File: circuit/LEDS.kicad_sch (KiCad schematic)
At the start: 22 parts, among them U801 74HC595, U802 74HC595

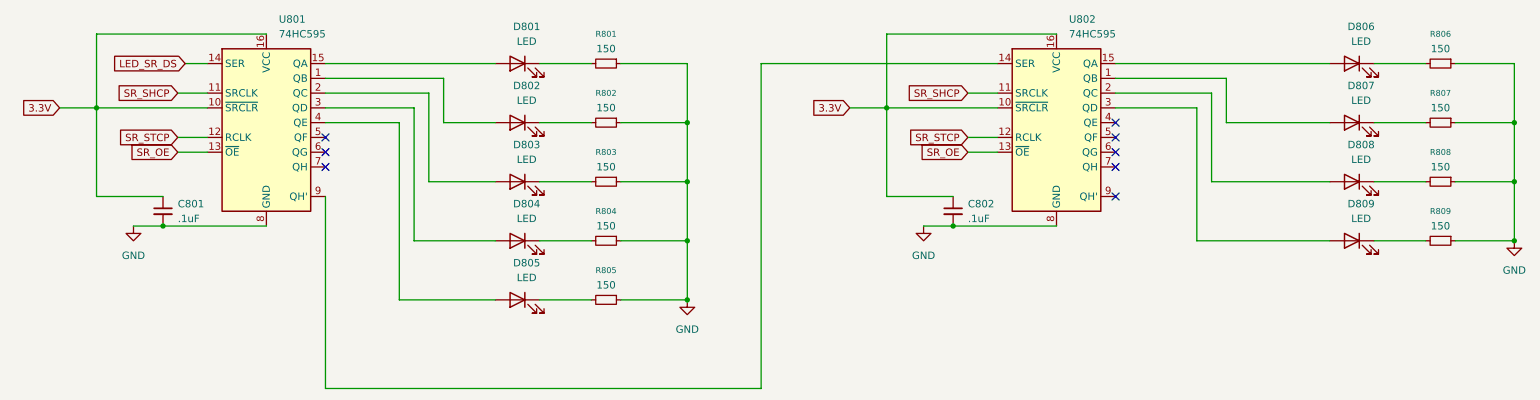
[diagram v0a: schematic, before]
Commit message: Very tentative PCB layout, Code compiles but needs major functionality testing.
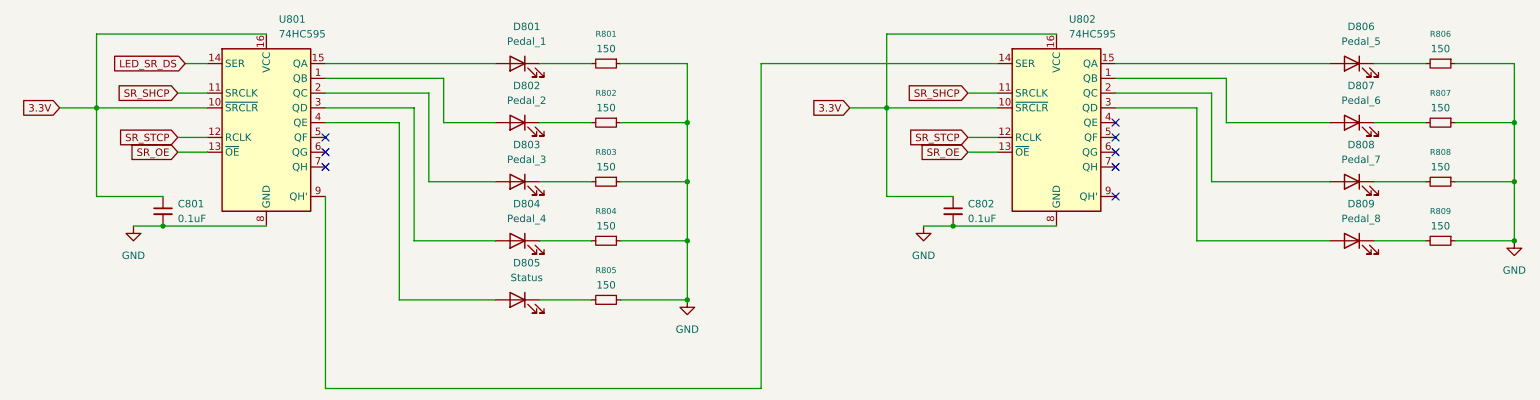
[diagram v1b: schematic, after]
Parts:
- C801, C802: value .1uF -> 0.1uF
- D801: value LED -> Pedal_1
- D802: value LED -> Pedal_2
- D803: value LED -> Pedal_3
- D804: value LED -> Pedal_4
- D805: value LED -> Status
- D806: value LED -> Pedal_5
- D807: value LED -> Pedal_6
- D808: value LED -> Pedal_7
- D809: value LED -> Pedal_8
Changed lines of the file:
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@@
 			)
 		)
-		(property "Value" "LED"
+		(property "Value" "Pedal_2"
 			(at 100.6475 72.39 0)
 			(effects
@@
 			)
 		)
-		(property "Value" ".1uF"
+		(property "Value" "0.1uF"
 			(at 40.64 92.7162 0)
 			(effects
@@
 			)
 		)
-		(property "Value" "LED"
+		(property "Value" "Pedal_7"
 			(at 244.1575 82.55 0)
 			(effects
@@
 			)
 		)
-		(property "Value" ".1uF"
+		(property "Value" "0.1uF"
 			(at 176.53 92.7162 0)
 			(effects
@@
 			)
 		)
-		(property "Value" "LED"
+		(property "Value" "Pedal_4"
 			(at 100.6475 92.71 0)
 			(effects
@@
 			)
 		)
-		(property "Value" "LED"
+		(property "Value" "Pedal_1"
 			(at 100.6475 62.23 0)
 			(effects
@@
 			)
 		)
-		(property "Value" "LED"
+		(property "Value" "Pedal_8"
 			(at 244.1575 92.71 0)
 			(effects
@@
 			)
 		)
-		(property "Value" "LED"
+		(property "Value" "Pedal_3"
 			(at 100.6475 82.55 0)
 			(effects
@@
 			)
 		)
-		(property "Value" "LED"
+		(property "Value" "Pedal_6"
 			(at 244.1575 72.39 0)
 			(effects
@@
 			)
 		)
-		(property "Value" "LED"
+		(property "Value" "Status"
 			(at 100.6475 102.87 0)
 			(effects
@@
 			)
 		)
-		(property "Value" "LED"
+		(property "Value" "Pedal_5"
 			(at 244.1575 62.23 0)
 			(effects

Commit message: Added ferrite beads and tweaked PCB
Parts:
- C801, C802: footprint Capacitor_THT:C_Axial_L3.8mm_D2.6mm_P7.50mm_Horizontal -> Capacitor_THT:C_Disc_D3.0mm_W2.0mm_P2.50mm
- D801, D802, D803, D804, D805, D806, D807, D808, D809: footprint Connector_Wire:SolderWire-0.1sqmm_1x02_P3.6mm_D0.4mm_OD1mm -> Connector_PinHeader_2.54mm:PinHeader_1x02_P2.54mm_Vertical
- R801, R802, R803, R804, R805, R806, R807, R808, R809: footprint Resistor_THT:R_Axial_DIN0204_L3.6mm_D1.6mm_P5.08mm_Horizontal -> Resistor_THT:R_Axial_DIN0207_L6.3mm_D2.5mm_P7.62mm_Horizontal
- U801, U802: footprint Package_DIP:CERDIP-16_W7.62mm_SideBrazed -> Package_DIP:DIP-16_W7.62mm
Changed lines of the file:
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@@
 			)
 		)
-		(property "Footprint" "Resistor_THT:R_Axial_DIN0204_L3.6mm_D1.6mm_P5.08mm_Horizontal"
+		(property "Footprint" "Resistor_THT:R_Axial_DIN0207_L6.3mm_D2.5mm_P7.62mm_Horizontal"
 			(at 114.3 106.68 0)
 			(effects
@@
 			)
 		)
-		(property "Footprint" "Resistor_THT:R_Axial_DIN0204_L3.6mm_D1.6mm_P5.08mm_Horizontal"
+		(property "Footprint" "Resistor_THT:R_Axial_DIN0207_L6.3mm_D2.5mm_P7.62mm_Horizontal"
 			(at 114.3 96.52 0)
 			(effects
@@
 			)
 		)
-		(property "Footprint" "Connector_Wire:SolderWire-0.1sqmm_1x02_P3.6mm_D0.4mm_OD1mm"
+		(property "Footprint" "Connector_PinHeader_2.54mm:PinHeader_1x02_P2.54mm_Vertical"
 			(at 99.06 76.2 0)
 			(effects
@@
 			)
 		)
-		(property "Description" "Light emitting diode"
+		(property "Description" ""
 			(at 99.06 76.2 0)
 			(effects
@@
 			)
 		)
-		(property "Footprint" "Resistor_THT:R_Axial_DIN0204_L3.6mm_D1.6mm_P5.08mm_Horizontal"
+		(property "Footprint" "Resistor_THT:R_Axial_DIN0207_L6.3mm_D2.5mm_P7.62mm_Horizontal"
 			(at 257.81 76.2 0)
 			(effects
@@
 			)
 		)
-		(property "Footprint" "Capacitor_THT:C_Axial_L3.8mm_D2.6mm_P7.50mm_Horizontal"
+		(property "Footprint" "Capacitor_THT:C_Disc_D3.0mm_W2.0mm_P2.50mm"
 			(at 38.1 91.44 0)
 			(effects
@@
 			)
 		)
-		(property "Footprint" "Connector_Wire:SolderWire-0.1sqmm_1x02_P3.6mm_D0.4mm_OD1mm"
+		(property "Footprint" "Connector_PinHeader_2.54mm:PinHeader_1x02_P2.54mm_Vertical"
 			(at 242.57 86.36 0)
 			(effects
@@
 			)
 		)
-		(property "Description" "Light emitting diode"
+		(property "Description" ""
 			(at 242.57 86.36 0)
 			(effects
@@
 			)
 		)
-		(property "Footprint" "Capacitor_THT:C_Axial_L3.8mm_D2.6mm_P7.50mm_Horizontal"
+		(property "Footprint" "Capacitor_THT:C_Disc_D3.0mm_W2.0mm_P2.50mm"
 			(at 173.99 91.44 0)
 			(effects
@@
 			)
 		)
-		(property "Footprint" "Resistor_THT:R_Axial_DIN0204_L3.6mm_D1.6mm_P5.08mm_Horizontal"
+		(property "Footprint" "Resistor_THT:R_Axial_DIN0207_L6.3mm_D2.5mm_P7.62mm_Horizontal"
 			(at 114.3 66.04 0)
 			(effects
@@
 			)
 		)
-		(property "Footprint" "Connector_Wire:SolderWire-0.1sqmm_1x02_P3.6mm_D0.4mm_OD1mm"
+		(property "Footprint" "Connector_PinHeader_2.54mm:PinHeader_1x02_P2.54mm_Vertical"
 			(at 99.06 96.52 0)
 			(effects
@@
 			)
 		)
-		(property "Description" "Light emitting diode"
+		(property "Description" ""
 			(at 99.06 96.52 0)
 			(effects
@@
 			)
 		)
-		(property "Footprint" "Connector_Wire:SolderWire-0.1sqmm_1x02_P3.6mm_D0.4mm_OD1mm"
+		(property "Footprint" "Connector_PinHeader_2.54mm:PinHeader_1x02_P2.54mm_Vertical"
 			(at 99.06 66.04 0)
 			(effects
@@
 			)
 		)
-		(property "Description" "Light emitting diode"
+		(property "Description" ""
 			(at 99.06 66.04 0)
 			(effects
@@
 			)
 		)
-		(property "Footprint" "Connector_Wire:SolderWire-0.1sqmm_1x02_P3.6mm_D0.4mm_OD1mm"
+		(property "Footprint" "Connector_PinHeader_2.54mm:PinHeader_1x02_P2.54mm_Vertical"
 			(at 242.57 96.52 0)
 			(effects
@@
 			)
 		)
-		(property "Description" "Light emitting diode"
+		(property "Description" ""
 			(at 242.57 96.52 0)
 			(effects
@@
 			)
 		)
-		(property "Footprint" "Connector_Wire:SolderWire-0.1sqmm_1x02_P3.6mm_D0.4mm_OD1mm"
+		(property "Footprint" "Connector_PinHeader_2.54mm:PinHeader_1x02_P2.54mm_Vertical"
 			(at 99.06 86.36 0)
 			(effects
@@
 			)
 		)
-		(property "Description" "Light emitting diode"
+		(property "Description" ""
 			(at 99.06 86.36 0)
 			(effects
@@
 			)
 		)
-		(property "Footprint" "Connector_Wire:SolderWire-0.1sqmm_1x02_P3.6mm_D0.4mm_OD1mm"
+		(property "Footprint" "Connector_PinHeader_2.54mm:PinHeader_1x02_P2.54mm_Vertical"
 			(at 242.57 76.2 0)
 			(effects
@@
 			)
 		)
-		(property "Description" "Light emitting diode"
+		(property "Description" ""
 			(at 242.57 76.2 0)
 			(effects
@@
 			)
 		)
-		(property "Footprint" "Resistor_THT:R_Axial_DIN0204_L3.6mm_D1.6mm_P5.08mm_Horizontal"
+		(property "Footprint" "Resistor_THT:R_Axial_DIN0207_L6.3mm_D2.5mm_P7.62mm_Horizontal"
 			(at 257.81 96.52 0)
 			(effects
@@
 			)
 		)
-		(property "Footprint" "Resistor_THT:R_Axial_DIN0204_L3.6mm_D1.6mm_P5.08mm_Horizontal"
+		(property "Footprint" "Resistor_THT:R_Axial_DIN0207_L6.3mm_D2.5mm_P7.62mm_Horizontal"
 			(at 114.3 86.36 0)
 			(effects
@@
 			)
 		)
-		(property "Footprint" "Connector_Wire:SolderWire-0.1sqmm_1x02_P3.6mm_D0.4mm_OD1mm"
+		(property "Footprint" "Connector_PinHeader_2.54mm:PinHeader_1x02_P2.54mm_Vertical"
 			(at 99.06 106.68 0)
 			(effects
@@
 			)
 		)
-		(property "Description" "Light emitting diode"
+		(property "Description" ""
 			(at 99.06 106.68 0)
 			(effects
@@
 			)
 		)
-		(property "Footprint" "Resistor_THT:R_Axial_DIN0204_L3.6mm_D1.6mm_P5.08mm_Horizontal"
+		(property "Footprint" "Resistor_THT:R_Axial_DIN0207_L6.3mm_D2.5mm_P7.62mm_Horizontal"
 			(at 257.81 66.04 0)
 			(effects
@@
 			)
 		)
-		(property "Footprint" "Connector_Wire:SolderWire-0.1sqmm_1x02_P3.6mm_D0.4mm_OD1mm"
+		(property "Footprint" "Connector_PinHeader_2.54mm:PinHeader_1x02_P2.54mm_Vertical"
 			(at 242.57 66.04 0)
 			(effects
@@
 			)
 		)
-		(property "Description" "Light emitting diode"
+		(property "Description" ""
 			(at 242.57 66.04 0)
 			(effects
@@
 			)
 		)
-		(property "Footprint" "Resistor_THT:R_Axial_DIN0204_L3.6mm_D1.6mm_P5.08mm_Horizontal"
+		(property "Footprint" "Resistor_THT:R_Axial_DIN0207_L6.3mm_D2.5mm_P7.62mm_Horizontal"
 			(at 257.81 86.36 0)
 			(effects
@@
 			)
 		)
-		(property "Footprint" "Package_DIP:CERDIP-16_W7.62mm_SideBrazed"
+		(property "Footprint" "Package_DIP:DIP-16_W7.62mm"
 			(at 191.77 76.2 0)
 			(effects
@@
 			)
 		)
-		(property "Footprint" "Resistor_THT:R_Axial_DIN0204_L3.6mm_D1.6mm_P5.08mm_Horizontal"
+		(property "Footprint" "Resistor_THT:R_Axial_DIN0207_L6.3mm_D2.5mm_P7.62mm_Horizontal"
 			(at 114.3 76.2 0)
 			(effects
@@
 			)
 		)
-		(property "Footprint" "Package_DIP:CERDIP-16_W7.62mm_SideBrazed"
+		(property "Footprint" "Package_DIP:DIP-16_W7.62mm"
 			(at 55.88 76.2 0)
 			(effects

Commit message: Circuit tweaks and PCB
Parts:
- C801, C802: footprint Capacitor_THT:C_Disc_D3.0mm_W2.0mm_P2.50mm -> Capacitor_THT:C_Disc_D5.0mm_W2.5mm_P2.50mm
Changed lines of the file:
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@@
 			)
 		)
-		(property "Footprint" "Capacitor_THT:C_Disc_D3.0mm_W2.0mm_P2.50mm"
+		(property "Footprint" "Capacitor_THT:C_Disc_D5.0mm_W2.5mm_P2.50mm"
 			(at 38.1 91.44 0)
 			(effects
@@
 			)
 		)
-		(property "Footprint" "Capacitor_THT:C_Disc_D3.0mm_W2.0mm_P2.50mm"
+		(property "Footprint" "Capacitor_THT:C_Disc_D5.0mm_W2.5mm_P2.50mm"
 			(at 173.99 91.44 0)
 			(effects
